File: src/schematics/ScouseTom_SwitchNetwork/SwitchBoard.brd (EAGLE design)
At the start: 169.5 x 97.5 mm, 87 parts, among them T1 PNP, U1 MCP73831, U10 ADG714BRUZ, U11 ADG714BRUZ, U12 ADUM1410ARWZ, U13 ADG714BRUZ, U14 ADG714BRUZ, U15 ADUM1412ARWZ, U2 ADG714BRUZ, U3 ADG714BRUZ, U4 TPS61090RSAR, U5 ADG714BRUZ, U6 ADG714BRUZ, U7 ADG714BRUZ, U8 LT1763CDE-5, U9 ADG714BRUZ, X1 USB-MICROB, X2 CTR_ARD, X3 CTR_OUT, X4 DSUB _T, X5 DSUB_B, X6 CTR_IN

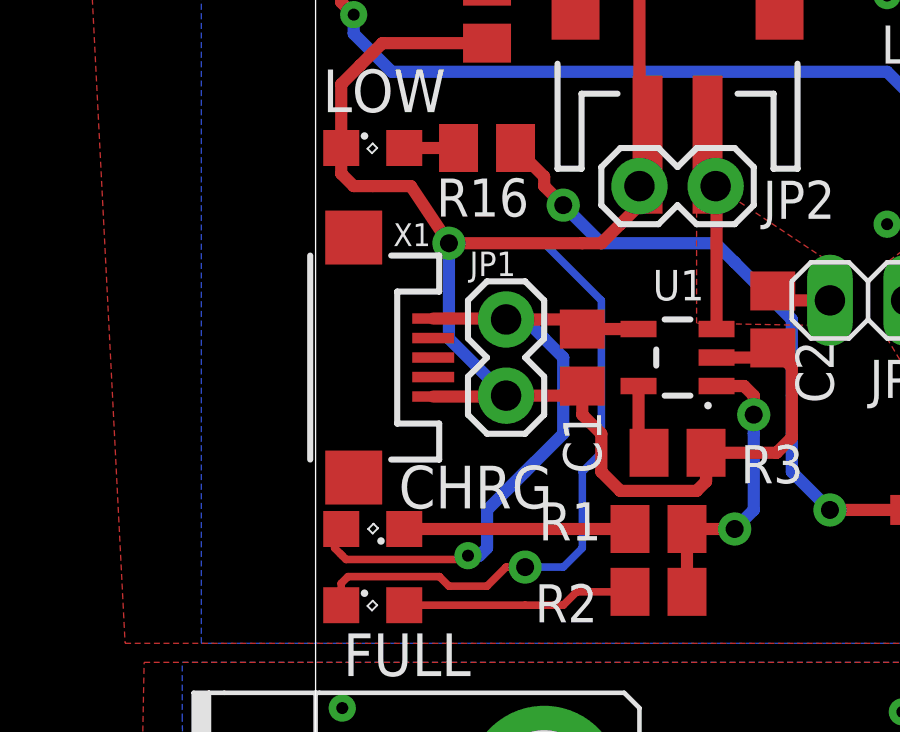
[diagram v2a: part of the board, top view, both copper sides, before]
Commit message: Changed USB connector on SwitchBoard
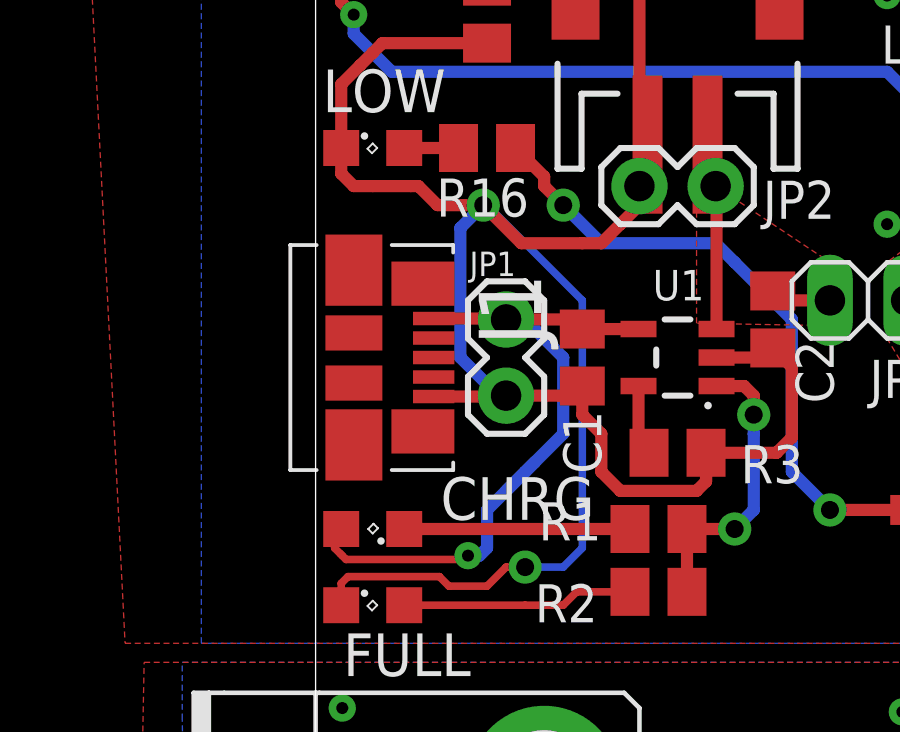
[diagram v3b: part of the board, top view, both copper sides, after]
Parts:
- removed X1: USB-MICROB, SparkFun:USB-MICROB
- added J1: (no value), Molex-47346-0001:MOLEX_47346-0001
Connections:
- net 5VIN: now also J1.1; no longer X1.VBUS
- net AGND: now also J1.5; no longer X1.GND
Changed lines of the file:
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@@
 <layer number="21" name="tPlace" color="16" fill="1" visible="yes" active="yes"/>
 <layer number="22" name="bPlace" color="14" fill="1" visible="yes" active="yes"/>
-<layer number="23" name="tOrigins" color="15" fill="1" visible="no" active="yes"/>
-<layer number="24" name="bOrigins" color="15" fill="1" visible="no" active="yes"/>
+<layer number="23" name="tOrigins" color="15" fill="1" visible="yes" active="yes"/>
+<layer number="24" name="bOrigins" color="15" fill="1" visible="yes" active="yes"/>
 <layer number="25" name="tNames" color="7" fill="1" visible="no" active="yes"/>
 <layer number="26" name="bNames" color="7" fill="1" visible="no" active="yes"/>
@@
 <text x="-0.508" y="42.545" size="1.6764" layer="21" font="vector" ratio="12" rot="R90" align="center">ARDUINO
 IN</text>
-<text x="-11.811" y="77.597" size="1.4224" layer="21" font="vector" ratio="16" align="center">CHRG</text>
+<text x="-10.414" y="77.216" size="1.4224" layer="21" font="vector" ratio="16" align="center">CHRG</text>
 <text x="-14.097" y="72.009" size="1.4224" layer="21" font="vector" ratio="16" align="center">FULL</text>
 <text x="-14.732" y="96.139" size="1.4224" layer="21" font="vector" ratio="16" align="center">PWR</text>
@@
 <attribute name="VALUE" x="-6.34995" y="92.709846875" size="0.4064" layer="27"/>
 </element>
-<element name="X1" library="SparkFun" package="USB-MICROB" value="USB-MICROB" x="-15.874340625" y="81.914746875" smashed="yes" rot="R270">
-<attribute name="NAME" x="-14.553746875" y="85.629659375" size="0.762" layer="25"/>
-<attribute name="VALUE" x="-19.049340625" y="83.819746875" size="0.762" layer="27" rot="R270"/>
-</element>
 <element name="JP1" library="SparkFun" package="1X02" value="IN" x="-10.79530625" y="83.184846875" smashed="yes" rot="R270">
 <attribute name="NAME" x="-12.014046875" y="84.63249375" size="0.8128" layer="25" ratio="10"/>
@@
 </element>
 <element name="U$1" library="pinhead" package="3X07" value="PINHD-3X7GAP" x="27.559" y="52.959" rot="R270"/>
+<element name="J1" library="Molex-47346-0001" package="MOLEX_47346-0001" value="" x="-13.208" y="81.915" rot="R270">
+<attribute name="PACKAGE" value="5 POS MICRO USB R/A" x="-13.208" y="81.915" size="1.778" layer="27" rot="R270" display="off"/>
+<attribute name="OC_NEWARK" value="47M0505" x="-13.208" y="81.915" size="1.778" layer="27" rot="R270" display="off"/>
+<attribute name="MPN" value="47346-0001" x="-13.208" y="81.915" size="1.778" layer="27" rot="R270" display="off"/>
+<attribute name="SUPPLIER" value="MOLEX" x="-13.208" y="81.915" size="1.778" layer="27" rot="R270" display="off"/>
+<attribute name="OC_FARNELL" value="1568026" x="-13.208" y="81.915" size="1.778" layer="27" rot="R270" display="off"/>
+</element>
 </elements>
 <signals>
@@
 <contactref element="R23" pad="1"/>
 <contactref element="R24" pad="1"/>
-<contactref element="X1" pad="GND"/>
 <contactref element="JP1" pad="2"/>
 <contactref element="U1" pad="2"/>
@@
 <contactref element="C10" pad="-"/>
 <contactref element="C15" pad="-"/>
-<wire x1="-13.224340625" y1="80.614746875" x2="-10.82540625" y2="80.614746875" width="0.4064" layer="1"/>
 <wire x1="-10.82540625" y1="80.614746875" x2="-10.79530625" y2="80.644846875" width="0.4064" layer="1"/>
 <wire x1="-10.79530625" y1="80.644846875" x2="-8.575153125" y2="80.644846875" width="0.4064" layer="1"/>
@@
 <wire x1="16.18969375" y1="43.815" x2="15.24" y2="43.815" width="0.4064" layer="1"/>
 <wire x1="-15.24" y1="87.63" x2="-13.97" y2="87.63" width="0.4064" layer="1"/>
-<via x="-12.7" y="85.725" extent="1-16" drill="0.6"/>
-<wire x1="-12.7" y1="85.725" x2="-12.7" y2="82.549540625" width="0.4064" layer="16"/>
-<wire x1="-12.7" y1="82.549540625" x2="-10.79530625" y2="80.644846875" width="0.4064" layer="16"/>
-<wire x1="-12.7" y1="85.725" x2="-13.97" y2="87.63" width="0.4064" layer="1"/>
+<via x="-11.557" y="86.995" extent="1-16" drill="0.6"/>
 <wire x1="10.7" y1="82.86" x2="10.7" y2="83.51" width="0.4064" layer="1"/>
 <wire x1="10.7" y1="83.51" x2="10.7" y2="84.16" width="0.4064" layer="1"/>
@@
 <wire x1="-6.985" y1="86.36" x2="-7.62" y2="85.725" width="0.4064" layer="1"/>
 <wire x1="-7.62" y1="85.725" x2="-8.255" y2="85.725" width="0.4064" layer="1"/>
-<wire x1="-8.255" y1="85.725" x2="-12.7" y2="85.725" width="0.4064" layer="1"/>
 <wire x1="-8.255" y1="80.965" x2="-8.255" y2="80.01" width="0.4064" layer="1"/>
 <wire x1="-4.13" y1="77.785" x2="-4.13" y2="78.74" width="0.4064" layer="1"/>
@@
 <via x="-10.16" y="74.93" extent="1-16" drill="0.6"/>
 <wire x1="-10.16" y1="74.93" x2="-8.89" y2="74.93" width="0.254" layer="16"/>
-<wire x1="-8.89" y1="74.93" x2="-8.255" y2="75.565" width="0.254" layer="16"/>
-<wire x1="-8.255" y1="75.565" x2="-8.255" y2="78.105" width="0.254" layer="16"/>
-<wire x1="-8.255" y1="78.105" x2="-7.62" y2="78.74" width="0.254" layer="16"/>
-<wire x1="-7.62" y1="78.74" x2="-7.62" y2="83.82" width="0.254" layer="16"/>
-<wire x1="-7.62" y1="83.82" x2="-9.525" y2="85.725" width="0.254" layer="16"/>
-<wire x1="-9.525" y1="85.725" x2="-12.7" y2="85.725" width="0.254" layer="16"/>
 <wire x1="22.225" y1="81.28" x2="19.05" y2="78.105" width="0.4064" layer="1"/>
 <wire x1="19.05" y1="78.105" x2="16.825" y2="78.105" width="0.4064" layer="1"/>
@@
 <wire x1="16.825" y1="78.105" x2="16.825" y2="76.896" width="0.4064" layer="1"/>
 <wire x1="16.825" y1="76.896" x2="15.494" y2="75.565" width="0.4064" layer="1"/>
+<contactref element="J1" pad="5"/>
+<wire x1="-13.208" y1="80.615" x2="-10.825153125" y2="80.615" width="0.4064" layer="1"/>
+<wire x1="-10.825153125" y1="80.615" x2="-10.79530625" y2="80.644846875" width="0.4064" layer="1"/>
+<wire x1="-13.97" y1="87.63" x2="-13.716" y2="87.63" width="0.4064" layer="1"/>
+<wire x1="-13.716" y1="87.63" x2="-13.081" y2="86.995" width="0.4064" layer="1"/>
+<wire x1="-13.081" y1="86.995" x2="-11.557" y2="86.995" width="0.4064" layer="1"/>
+<wire x1="-8.255" y1="85.725" x2="-10.287" y2="85.725" width="0.4064" layer="1"/>
+<wire x1="-10.287" y1="85.725" x2="-11.557" y2="86.995" width="0.4064" layer="1"/>
+<wire x1="-10.79530625" y1="80.644846875" x2="-11.048846875" y2="80.644846875" width="0.4064" layer="16"/>
+<wire x1="-11.048846875" y1="80.644846875" x2="-12.319" y2="81.915" width="0.4064" layer="16"/>
+<wire x1="-12.319" y1="81.915" x2="-12.319" y2="86.233" width="0.4064" layer="16"/>
+<wire x1="-12.319" y1="86.233" x2="-11.557" y2="86.995" width="0.4064" layer="16"/>
+<wire x1="-8.89" y1="74.93" x2="-8.255" y2="75.565" width="0.254" layer="16"/>
+<wire x1="-8.255" y1="75.565" x2="-8.255" y2="83.82" width="0.254" layer="16"/>
+<wire x1="-8.255" y1="83.82" x2="-11.43" y2="86.995" width="0.254" layer="16"/>
+<wire x1="-11.43" y1="86.995" x2="-11.557" y2="86.995" width="0.254" layer="16"/>
 </signal>
 <signal name="SCLK">
@@
 <signal name="5VIN">
 <contactref element="U1" pad="4"/>
-<contactref element="X1" pad="VBUS"/>
 <contactref element="JP1" pad="1"/>
 <contactref element="C1" pad="1"/>
 <contactref element="LED1" pad="A"/>
-<wire x1="-13.224340625" y1="83.214746875" x2="-10.82520625" y2="83.214746875" width="0.4064" layer="1"/>
-<wire x1="-10.82520625" y1="83.214746875" x2="-10.79530625" y2="83.184846875" width="0.4064" layer="1"/>
 <wire x1="-10.79530625" y1="83.184846875" x2="-8.574846875" y2="83.184846875" width="0.4064" layer="1"/>
 <wire x1="-8.574846875" y1="83.184846875" x2="-8.255" y2="82.865" width="0.4064" layer="1"/>
@@
 <wire x1="-16.129" y1="75.184" x2="-12.192" y2="75.184" width="0.254" layer="1"/>
 <wire x1="-12.192" y1="75.184" x2="-12.065" y2="75.311" width="0.254" layer="1"/>
+<contactref element="J1" pad="1"/>
+<wire x1="-13.208" y1="83.215" x2="-10.825459375" y2="83.215" width="0.4064" layer="1"/>
+<wire x1="-10.825459375" y1="83.215" x2="-10.79530625" y2="83.184846875" width="0.4064" layer="1"/>
 </signal>
 <signal name="VBATT_B">

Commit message: Files ready to send to PCBTrain
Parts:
- renumbered J1 to X1
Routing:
- removed copper zone on layer 1, net N$3
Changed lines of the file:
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@@
 <layer number="20" name="Dimension" color="15" fill="1" visible="yes" active="yes"/>
 <layer number="21" name="tPlace" color="16" fill="1" visible="yes" active="yes"/>
-<layer number="22" name="bPlace" color="14" fill="1" visible="yes" active="yes"/>
+<layer number="22" name="bPlace" color="14" fill="1" visible="no" active="yes"/>
 <layer number="23" name="tOrigins" color="15" fill="1" visible="yes" active="yes"/>
-<layer number="24" name="bOrigins" color="15" fill="1" visible="yes" active="yes"/>
-<layer number="25" name="tNames" color="7" fill="1" visible="no" active="yes"/>
+<layer number="24" name="bOrigins" color="15" fill="1" visible="no" active="yes"/>
+<layer number="25" name="tNames" color="7" fill="1" visible="yes" active="yes"/>
 <layer number="26" name="bNames" color="7" fill="1" visible="no" active="yes"/>
 <layer number="27" name="tValues" color="7" fill="1" visible="no" active="yes"/>
@@
 <layer number="38" name="bTest" color="7" fill="1" visible="no" active="yes"/>
 <layer number="39" name="tKeepout" color="4" fill="11" visible="yes" active="yes"/>
-<layer number="40" name="bKeepout" color="1" fill="11" visible="yes" active="yes"/>
-<layer number="41" name="tRestrict" color="4" fill="10" visible="no" active="yes"/>
+<layer number="40" name="bKeepout" color="1" fill="11" visible="no" active="yes"/>
+<layer number="41" name="tRestrict" color="4" fill="10" visible="yes" active="yes"/>
 <layer number="42" name="bRestrict" color="1" fill="10" visible="no" active="yes"/>
 <layer number="43" name="vRestrict" color="2" fill="10" visible="no" active="yes"/>
@@
 <text x="-0.508" y="42.545" size="1.6764" layer="21" font="vector" ratio="12" rot="R90" align="center">ARDUINO
 IN</text>
-<text x="-10.414" y="77.216" size="1.4224" layer="21" font="vector" ratio="16" align="center">CHRG</text>
+<text x="-10.414" y="76.962" size="1.4224" layer="21" font="vector" ratio="16" align="center">CHRG</text>
 <text x="-14.097" y="72.009" size="1.4224" layer="21" font="vector" ratio="16" align="center">FULL</text>
 <text x="-14.732" y="96.139" size="1.4224" layer="21" font="vector" ratio="16" align="center">PWR</text>
@@
 </element>
 <element name="JP1" library="SparkFun" package="1X02" value="IN" x="-10.79530625" y="83.184846875" smashed="yes" rot="R270">
-<attribute name="NAME" x="-12.014046875" y="84.63249375" size="0.8128" layer="25" ratio="10"/>
+<attribute name="NAME" x="-11.633046875" y="84.75949375" size="0.8128" layer="25" ratio="10"/>
 <attribute name="VALUE" x="-13.97030625" y="84.454846875" size="1.27" layer="27" rot="R270"/>
 </element>
@@
 <attribute name="MF" value="" x="24.13" y="91.44" size="1.778" layer="27" rot="R90" display="off"/>
 <attribute name="OC_FARNELL" value="1556468" x="24.13" y="91.44" size="1.778" layer="27" rot="R90" display="off"/>
-<attribute name="NAME" x="23.852" y="94.905" size="1.27" layer="25" rot="R180"/>
+<attribute name="NAME" x="25.122" y="96.048" size="1.27" layer="25" rot="R180"/>
 <attribute name="VALUE" x="25.63" y="94.815" size="1.27" layer="27" rot="R180"/>
 </element>
@@
 </element>
 <element name="C2" library="resistor" package="C0805" value="10uF" x="-1.905" y="83.185" smashed="yes" rot="R270">
-<attribute name="NAME" x="0.127" y="80.391" size="1.27" layer="25" rot="R90"/>
+<attribute name="NAME" x="0.635" y="79.883" size="1.27" layer="25" rot="R90"/>
 <attribute name="VALUE" x="-4.445" y="84.455" size="1.27" layer="27" rot="R270"/>
 </element>
@@
 </element>
 <element name="R1" library="rcl" package="M0805" value="470" x="-5.715" y="76.2" smashed="yes" rot="R180">
-<attribute name="NAME" x="-7.62" y="77.089" size="1.27" layer="25" rot="R180"/>
+<attribute name="NAME" x="-2.413" y="77.343" size="1.27" layer="25" rot="R270"/>
 <attribute name="VALUE" x="-4.445" y="78.74" size="1.27" layer="27" rot="R180"/>
 </element>
 <element name="R2" library="rcl" package="M0805" value="1k" x="-5.715" y="74.1045" smashed="yes" rot="R180">
-<attribute name="NAME" x="-7.747" y="74.3585" size="1.27" layer="25" rot="R180"/>
+<attribute name="NAME" x="-3.556" y="73.5965" size="1.27" layer="25"/>
 <attribute name="VALUE" x="-4.445" y="76.6445" size="1.27" layer="27" rot="R180"/>
 </element>
@@
 </element>
 <element name="C15" library="rcl" package="CT6032" value="100uF" x="26.67" y="86.995" smashed="yes" rot="R180">
-<attribute name="NAME" x="27.051" y="84.709" size="1.27" layer="25" rot="R180"/>
+<attribute name="NAME" x="27.559" y="84.709" size="1.27" layer="25" rot="R270"/>
 <attribute name="VALUE" x="29.21" y="90.17" size="1.27" layer="27" rot="R180"/>
 </element>
@@
 <attribute name="VALUE" x="136.525" y="76.2" size="1.27" layer="27"/>
 </element>
-<element name="U$1" library="pinhead" package="3X07" value="PINHD-3X7GAP" x="27.559" y="52.959" rot="R270"/>
-<element name="J1" library="Molex-47346-0001" package="MOLEX_47346-0001" value="" x="-13.208" y="81.915" rot="R270">
+<element name="U$1" library="pinhead" package="3X07" value="PINHD-3X7GAP" x="27.559" y="52.959" smashed="yes" rot="R270">
+<attribute name="NAME" x="22.225" y="58.928" size="1.27" layer="25" ratio="10" rot="R90"/>
+<attribute name="VALUE" x="20.574" y="61.849" size="1.27" layer="27" rot="R270"/>
+</element>
+<element name="X1" library="Molex-47346-0001" package="MOLEX_47346-0001" value="" x="-13.208" y="81.915" smashed="yes" rot="R270">
 <attribute name="PACKAGE" value="5 POS MICRO USB R/A" x="-13.208" y="81.915" size="1.778" layer="27" rot="R270" display="off"/>
 <attribute name="OC_NEWARK" value="47M0505" x="-13.208" y="81.915" size="1.778" layer="27" rot="R270" display="off"/>
@@
 <attribute name="SUPPLIER" value="MOLEX" x="-13.208" y="81.915" size="1.778" layer="27" rot="R270" display="off"/>
 <attribute name="OC_FARNELL" value="1568026" x="-13.208" y="81.915" size="1.778" layer="27" rot="R270" display="off"/>
+<attribute name="NAME" x="-16.008" y="86.463" size="1.27" layer="25" ratio="10"/>
+<attribute name="VALUE" x="-20.808" y="85.115" size="2.0828" layer="27" ratio="10" rot="R270"/>
 </element>
 </elements>
@@
 <wire x1="16.825" y1="78.105" x2="16.825" y2="76.896" width="0.4064" layer="1"/>
 <wire x1="16.825" y1="76.896" x2="15.494" y2="75.565" width="0.4064" layer="1"/>
-<contactref element="J1" pad="5"/>
+<contactref element="X1" pad="5"/>
 <wire x1="-13.208" y1="80.615" x2="-10.825153125" y2="80.615" width="0.4064" layer="1"/>
 <wire x1="-10.825153125" y1="80.615" x2="-10.79530625" y2="80.644846875" width="0.4064" layer="1"/>
@@
 <wire x1="-16.129" y1="75.184" x2="-12.192" y2="75.184" width="0.254" layer="1"/>
 <wire x1="-12.192" y1="75.184" x2="-12.065" y2="75.311" width="0.254" layer="1"/>
-<contactref element="J1" pad="1"/>
+<contactref element="X1" pad="1"/>
 <wire x1="-13.208" y1="83.215" x2="-10.825459375" y2="83.215" width="0.4064" layer="1"/>
 <wire x1="-10.825459375" y1="83.215" x2="-10.79530625" y2="83.184846875" width="0.4064" layer="1"/>
@@
 <vertex x="9.525" y="82.169"/>
 </polygon>
-<polygon width="0" layer="1" thermals="no">
-<vertex x="5.588" y="77.2795"/>
-<vertex x="6.223" y="77.1525"/>
-<vertex x="6.223" y="78.4225"/>
-<vertex x="5.588" y="78.2955"/>
-</polygon>
 <polygon width="0.254" layer="1" thermals="no">
 <vertex x="4.445" y="86.995"/>
@@
 <wire x1="27.055" y1="91.19" x2="27.94" y2="92.075" width="0.254" layer="1"/>
 <wire x1="27.94" y1="92.075" x2="27.94" y2="92.395" width="0.254" layer="1"/>
-<polygon width="0" layer="1" thermals="no">
-<vertex x="26.416" y="92.202"/>
-<vertex x="27.7495" y="92.202"/>
-<vertex x="27.6225" y="91.694"/>
-<vertex x="27.051" y="91.186"/>
-<vertex x="26.416" y="91.186"/>
-</polygon>
 </signal>
 <signal name="N$4">
